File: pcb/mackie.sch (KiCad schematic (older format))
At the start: 28 parts, among them J1 Conn_01x05, SW1 SW_PUSH, SW2 SW_PUSH, U1 STM32F072CBTx, U2 TLV75533PDBV

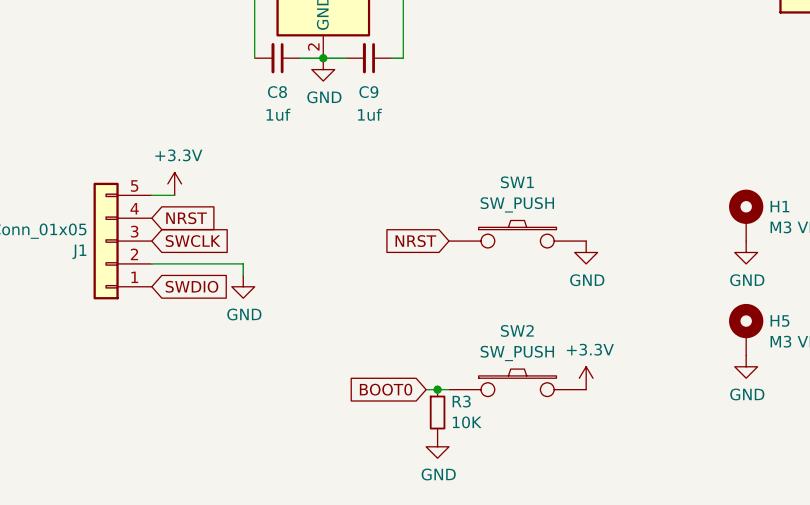
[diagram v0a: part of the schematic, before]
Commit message: added debouncing cap
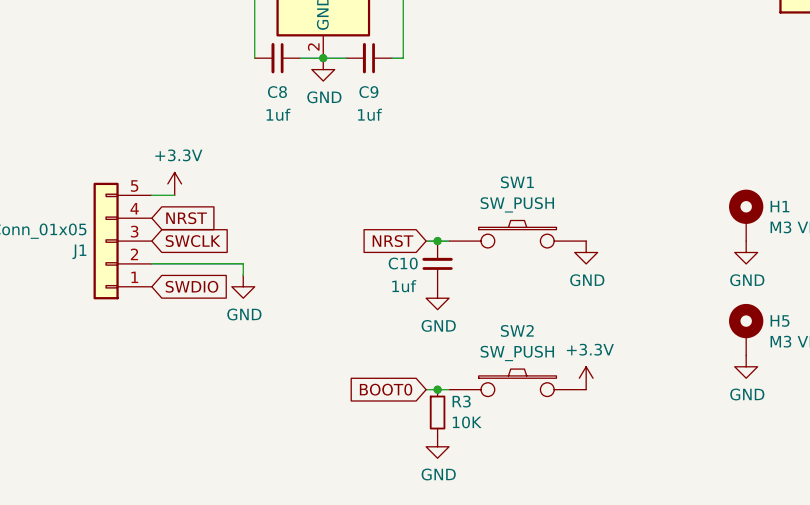
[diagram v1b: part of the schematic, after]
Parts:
- added C10: 1uf, Capacitor_SMD:C_0603_1608Metric, symbol Device:C_Small
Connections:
- net GND: now also C10.1
- net NRST: now also C10.2
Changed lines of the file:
@@
 EESchema Schematic File Version 4
+LIBS:mackie-cache
 EELAYER 29 0
 EELAYER END
@@
 Text GLabel 4150 11200 0    50   Input ~ 0
 BOOT0
-Text GLabel 2800 14700 0    50   Input ~ 0
+Text GLabel 2700 14700 0    50   Input ~ 0
 NRST
 $Comp
@@
 Wire Wire Line
 	2600 13500 2550 13500
+$Comp
+L Device:C_Small C10
+U 1 1 5D22204B
+P 2750 14800
+F 0 "C10" H 2900 14800 50  0000 C CNN
+F 1 "1uf" H 2900 14900 50  0000 C CNN
+F 2 "Capacitor_SMD:C_0603_1608Metric" H 2750 14800 50  0001 C CNN
+F 3 "~" H 2750 14800 50  0001 C CNN
+	1    2750 14800
+	-1   0    0    1
+$EndComp
+Wire Wire Line
+	2700 14700 2750 14700
+Connection ~ 2750 14700
+Wire Wire Line
+	2750 14700 2800 14700
+$Comp
+L power:GND #PWR034
+U 1 1 5D22529A
+P 2750 14900
+F 0 "#PWR034" H 2750 14650 50  0001 C CNN
+F 1 "GND" H 2755 14727 50  0000 C CNN
+F 2 "" H 2750 14900 50  0001 C CNN
+F 3 "" H 2750 14900 50  0001 C CNN
+	1    2750 14900
+	1    0    0    -1
+$EndComp
 $EndSCHEMATC

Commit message: fucking with a switch matrix
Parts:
- added D1, D2, D3, D4, D5, D6: D_Small, Diode_SMD:D_SOD-123, symbol Device:D_Small
- added K1, K2, K3, K4, K5, K6: KEYSW, MX_SMK_2:Choc_Hotswap_1u, symbol keyboard_parts:KEYSW
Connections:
- new net: D1.2 (A), K1.2
- new net: D1.1 (K), D2.1 (K), D3.1 (K), D4.1 (K), D5.1 (K), D6.1 (K)
- new net: D2.2 (A), K2.2
- new net: D3.2 (A), K3.2
- new net: D4.2 (A), K4.2
- new net: D5.2 (A), K5.2
- new net: D6.2 (A), K6.2
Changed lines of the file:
@@
 	1    0    0    -1
 $EndComp
+$Comp
+L keyboard_parts:KEYSW K1
+U 1 1 5D3EB1F4
+P 7150 2500
+F 0 "K1" H 7150 2733 60  0000 C CNN
+F 1 "KEYSW" H 7150 2400 60  0001 C CNN
+F 2 "MX_SMK_2:Choc_Hotswap_1u" H 7150 2500 60  0001 C CNN
+F 3 "" H 7150 2500 60  0000 C CNN
+	1    7150 2500
+	1    0    0    -1
+$EndComp
+$Comp
+L Device:D_Small D1
+U 1 1 5D3EC05C
+P 6850 2600
+F 0 "D1" V 6896 2532 50  0000 R CNN
+F 1 "D_Small" V 6805 2532 50  0000 R CNN
+F 2 "Diode_SMD:D_SOD-123" V 6850 2600 50  0001 C CNN
+F 3 "~" V 6850 2600 50  0001 C CNN
+	1    6850 2600
+	0    -1   -1   0
+$EndComp
+$Comp
+L keyboard_parts:KEYSW K2
+U 1 1 5D3EDA78
+P 7900 2500
+F 0 "K2" H 7900 2733 60  0000 C CNN
+F 1 "KEYSW" H 7900 2400 60  0001 C CNN
+F 2 "MX_SMK_2:Choc_Hotswap_1u" H 7900 2500 60  0001 C CNN
+F 3 "" H 7900 2500 60  0000 C CNN
+	1    7900 2500
+	1    0    0    -1
+$EndComp
+$Comp
+L Device:D_Small D2
+U 1 1 5D3EDA7E
+P 7600 2600
+F 0 "D2" V 7646 2532 50  0000 R CNN
+F 1 "D_Small" V 7555 2532 50  0000 R CNN
+F 2 "Diode_SMD:D_SOD-123" V 7600 2600 50  0001 C CNN
+F 3 "~" V 7600 2600 50  0001 C CNN
+	1    7600 2600
+	0    -1   -1   0
+$EndComp
+$Comp
+L keyboard_parts:KEYSW K3
+U 1 1 5D3F0EE3
+P 8650 2500
+F 0 "K3" H 8650 2733 60  0000 C CNN
+F 1 "KEYSW" H 8650 2400 60  0001 C CNN
+F 2 "MX_SMK_2:Choc_Hotswap_1u" H 8650 2500 60  0001 C CNN
+F 3 "" H 8650 2500 60  0000 C CNN
+	1    8650 2500
+	1    0    0    -1
+$EndComp
+$Comp
+L Device:D_Small D3
+U 1 1 5D3F0EE9
+P 8350 2600
+F 0 "D3" V 8396 2532 50  0000 R CNN
+F 1 "D_Small" V 8305 2532 50  0000 R CNN
+F 2 "Diode_SMD:D_SOD-123" V 8350 2600 50  0001 C CNN
+F 3 "~" V 8350 2600 50  0001 C CNN
+	1    8350 2600
+	0    -1   -1   0
+$EndComp
+$Comp
+L keyboard_parts:KEYSW K4
+U 1 1 5D3F0EEF
+P 9400 2500
+F 0 "K4" H 9400 2733 60  0000 C CNN
+F 1 "KEYSW" H 9400 2400 60  0001 C CNN
+F 2 "MX_SMK_2:Choc_Hotswap_1u" H 9400 2500 60  0001 C CNN
+F 3 "" H 9400 2500 60  0000 C CNN
+	1    9400 2500
+	1    0    0    -1
+$EndComp
+$Comp
+L Device:D_Small D4
+U 1 1 5D3F0EF5
+P 9100 2600
+F 0 "D4" V 9146 2532 50  0000 R CNN
+F 1 "D_Small" V 9055 2532 50  0000 R CNN
+F 2 "Diode_SMD:D_SOD-123" V 9100 2600 50  0001 C CNN
+F 3 "~" V 9100 2600 50  0001 C CNN
+	1    9100 2600
+	0    -1   -1   0
+$EndComp
+$Comp
+L keyboard_parts:KEYSW K5
+U 1 1 5D3F53C6
+P 10150 2500
+F 0 "K5" H 10150 2733 60  0000 C CNN
+F 1 "KEYSW" H 10150 2400 60  0001 C CNN
+F 2 "MX_SMK_2:Choc_Hotswap_1u" H 10150 2500 60  0001 C CNN
+F 3 "" H 10150 2500 60  0000 C CNN
+	1    10150 2500
+	1    0    0    -1
+$EndComp
+$Comp
+L Device:D_Small D5
+U 1 1 5D3F53CC
+P 9850 2600
+F 0 "D5" V 9896 2532 50  0000 R CNN
+F 1 "D_Small" V 9805 2532 50  0000 R CNN
+F 2 "Diode_SMD:D_SOD-123" V 9850 2600 50  0001 C CNN
+F 3 "~" V 9850 2600 50  0001 C CNN
+	1    9850 2600
+	0    -1   -1   0
+$EndComp
+$Comp
+L keyboard_parts:KEYSW K6
+U 1 1 5D3F53D2
+P 10900 2500
+F 0 "K6" H 10900 2733 60  0000 C CNN
+F 1 "KEYSW" H 10900 2400 60  0001 C CNN
+F 2 "MX_SMK_2:Choc_Hotswap_1u" H 10900 2500 60  0001 C CNN
+F 3 "" H 10900 2500 60  0000 C CNN
+	1    10900 2500
+	1    0    0    -1
+$EndComp
+$Comp
+L Device:D_Small D6
+U 1 1 5D3F53D8
+P 10600 2600
+F 0 "D6" V 10646 2532 50  0000 R CNN
+F 1 "D_Small" V 10555 2532 50  0000 R CNN
+F 2 "Diode_SMD:D_SOD-123" V 10600 2600 50  0001 C CNN
+F 3 "~" V 10600 2600 50  0001 C CNN
+	1    10600 2600
+	0    -1   -1   0
+$EndComp
+Wire Wire Line
+	6850 2700 7600 2700
+Connection ~ 7600 2700
+Wire Wire Line
+	7600 2700 8350 2700
+Connection ~ 8350 2700
+Wire Wire Line
+	8350 2700 9100 2700
+Connection ~ 9100 2700
+Wire Wire Line
+	9100 2700 9850 2700
+Connection ~ 9850 2700
+Wire Wire Line
+	9850 2700 10600 2700
 $EndSCHEMATC
